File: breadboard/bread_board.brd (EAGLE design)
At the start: 40 x 50 mm, 7 parts, among them J2 DC_JACK

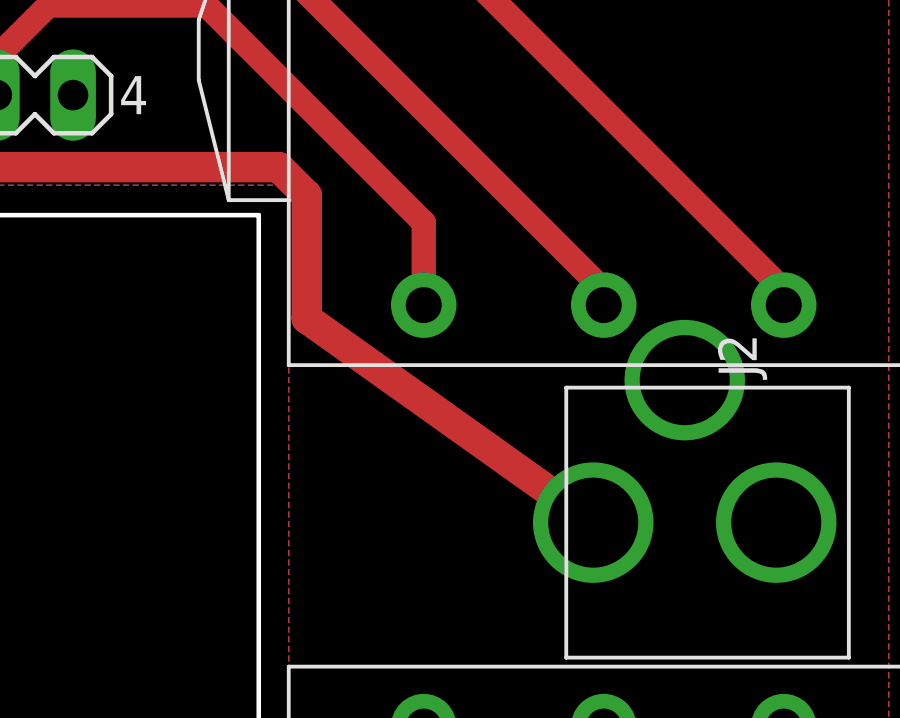
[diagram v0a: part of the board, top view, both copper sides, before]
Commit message: Updated or downgraded bread board
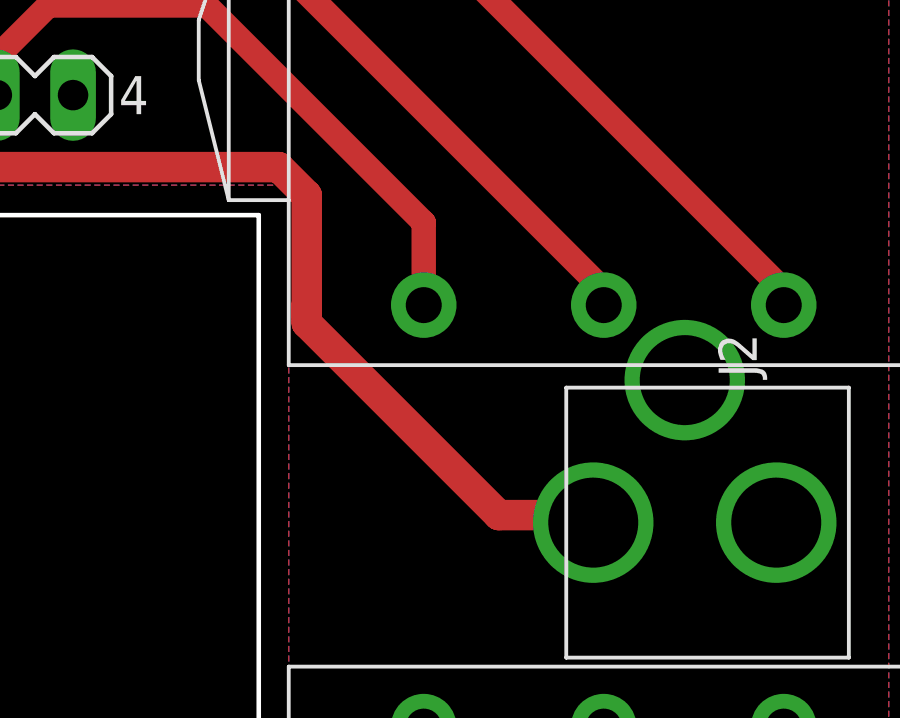
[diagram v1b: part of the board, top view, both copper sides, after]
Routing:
- net N$4: track 52.2 -> 53.4 mm
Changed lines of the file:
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@@
 <wire x1="-3" y1="37" x2="-2.6002" y2="36.6002" width="1.016" layer="1"/>
 <wire x1="13.662825" y1="36.6002" x2="14.6002" y2="35.662825" width="1.016" layer="1"/>
-<wire x1="14.6002" y1="31.5498" x2="24.15" y2="24.75" width="1.016" layer="1"/>
 <wire x1="-2.6002" y1="36.6002" x2="13.662825" y2="36.6002" width="1.016" layer="1"/>
-<wire x1="14.6002" y1="35.662825" x2="14.6002" y2="31.5498" width="1.016" layer="1"/>
+<wire x1="14.6002" y1="35.662825" x2="14.6002" y2="32" width="1.016" layer="1"/>
+<wire x1="14.6002" y1="32" x2="14.6002" y2="31.5498" width="1.016" layer="1"/>
+<wire x1="14.6002" y1="32" x2="14.6002" y2="31.3998" width="1.016" layer="1"/>
+<wire x1="14.6002" y1="31.3998" x2="21" y2="25" width="1.016" layer="1"/>
+<wire x1="21" y1="25" x2="23.9" y2="25" width="1.016" layer="1"/>
+<wire x1="23.9" y1="25" x2="24.15" y2="24.75" width="1.016" layer="1"/>
 </signal>
 <signal name="N$5">
